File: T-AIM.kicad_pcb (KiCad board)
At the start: 2 copper layers, 87.7 x 68.7 mm, 44 parts, among them IC1 ATMEGA328PB-A, J1 ADXL345 Connector, J2 PIR Sensor Connector, J3 JY-MCU HC-05 Pins, J4 CONN_01X03, J5 CONN_01X02, J6 CONN_01X03, SW1 Connection Button, SW2 Reset Button, U1 TPS61200

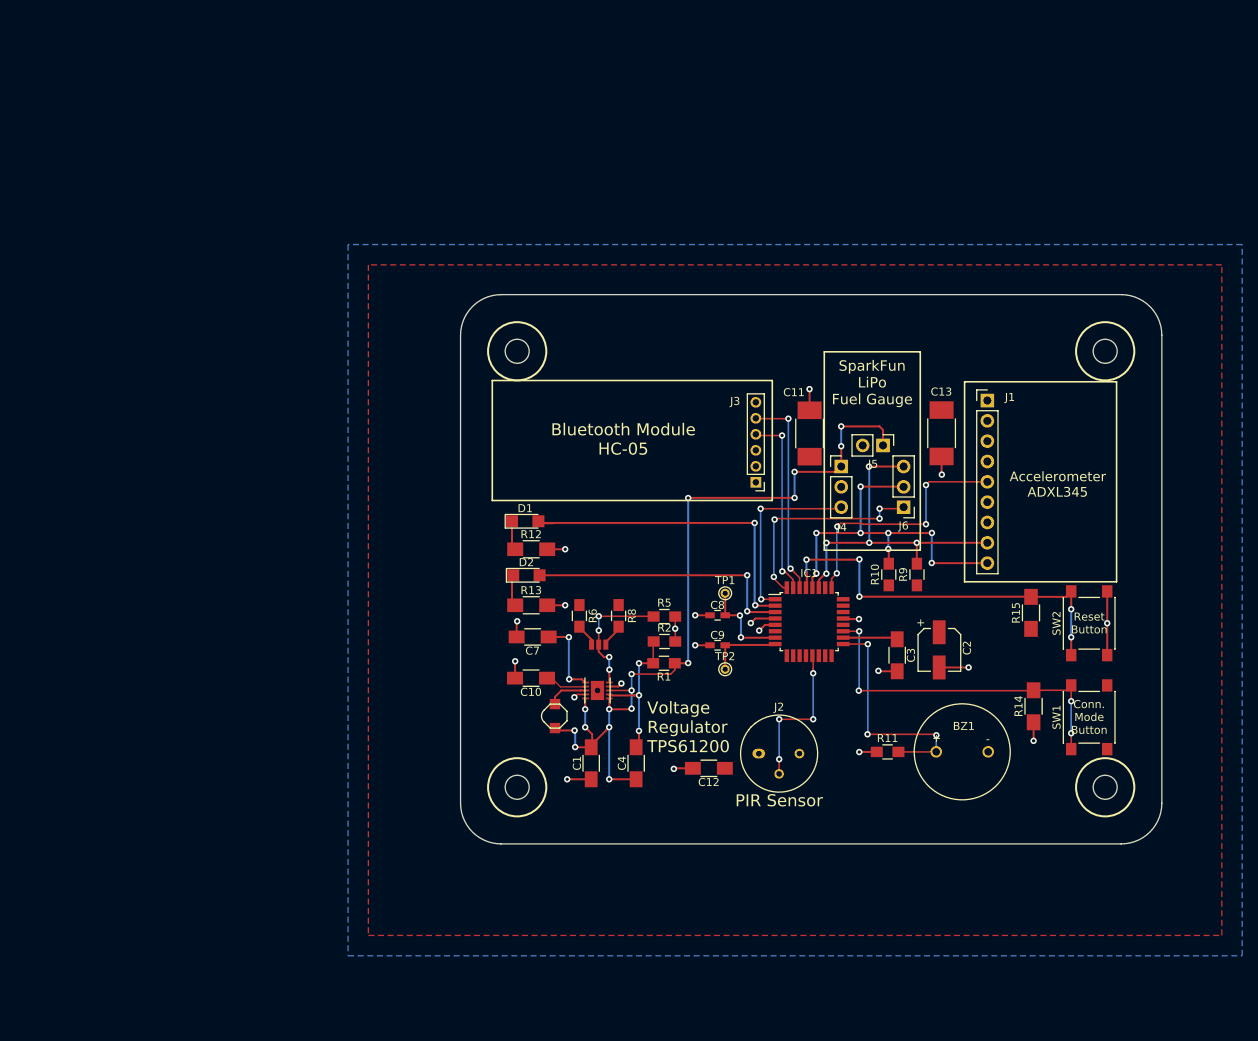
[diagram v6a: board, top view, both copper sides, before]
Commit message: v0.3: 3.9V field shrunk; Added ISP header; Fixed fuel gauge pin shortcut :P
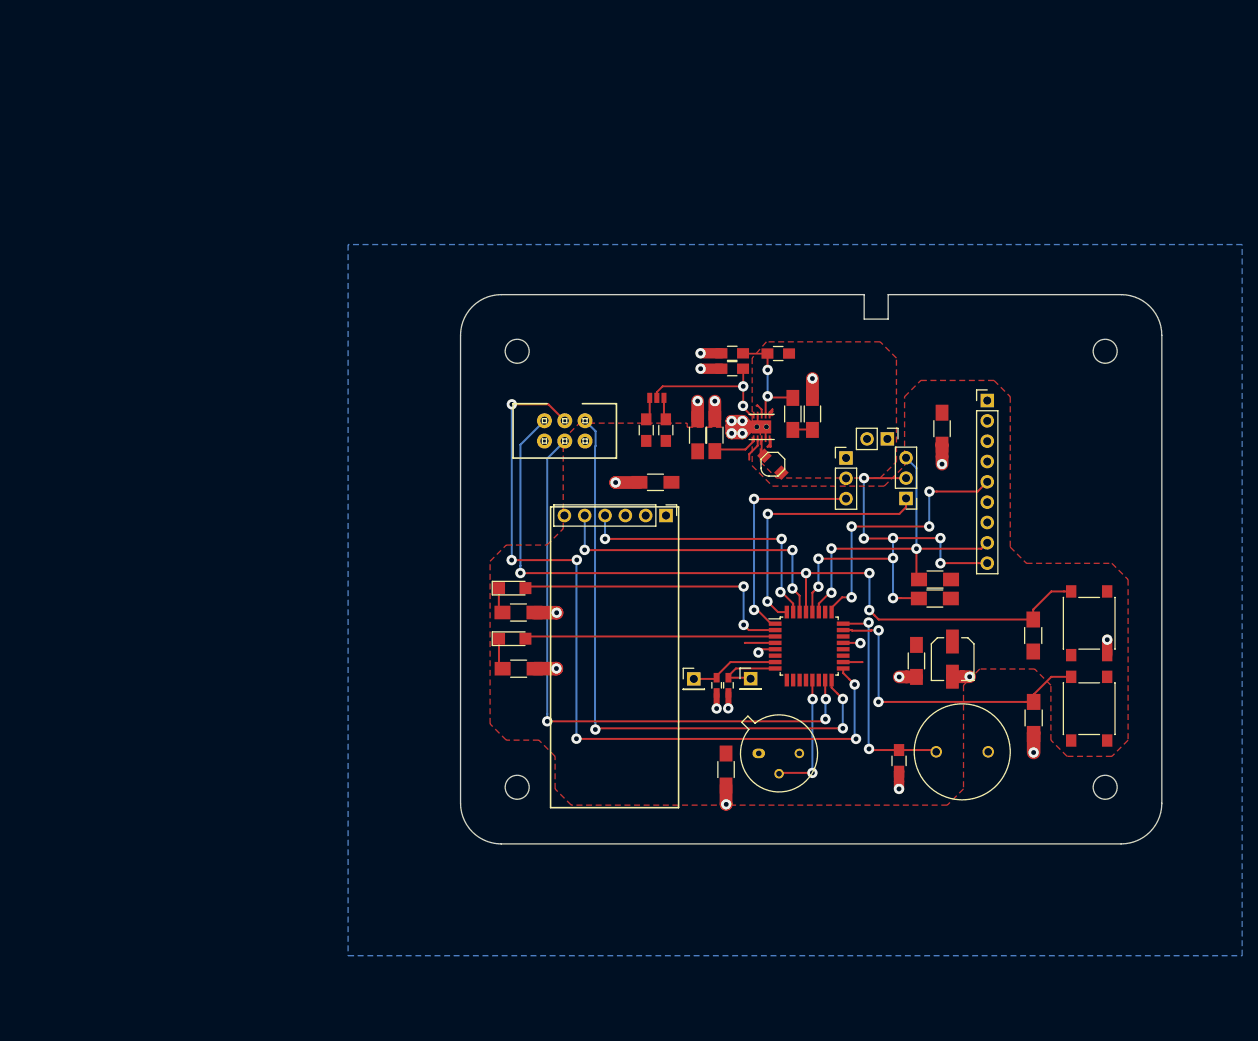
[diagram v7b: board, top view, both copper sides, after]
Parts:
- removed C12: 0.1uF, Capacitors_SMD:C_1206_HandSoldering
- removed C13: 0.1uF, Capacitors_SMD:C_1812_HandSoldering
- removed R13: 220, Resistors_SMD:R_1206_HandSoldering
- removed R14, R15: 10k, Resistors_SMD:R_1206_HandSoldering
- added C5: 0.1uF, Capacitors_SMD:C_1206_HandSoldering, F.Cu at (152.1, 69.8)
- added C6: 22pF, Capacitors_SMD:C_0603_HandSoldering, F.Cu at (152.3, 101.1)
- added CON1: AVR-ISP-6, T-AIM:2X3-SHROUDED, F.Cu at (133.3, 69.3)
- added R3: 220k, Resistors_SMD:R_0805_HandSoldering, F.Cu at (154.2, 61.5)
- added R4: 1.5M, Resistors_SMD:R_0805_HandSoldering, F.Cu at (145.9, 69.2)
- added R7: 10k, Resistors_SMD:R_1206_HandSoldering, F.Cu at (179.6, 90.2)
- C10: value 22uF -> 0.1uF
- C11: footprint Capacitors_SMD:C_1812_HandSoldering -> Capacitors_SMD:C_1206_HandSoldering
- C7: value 0.1uF -> 22pF; footprint Capacitors_SMD:C_1206_HandSoldering -> Capacitors_SMD:C_0603_HandSoldering
- C8: value 22pF -> 22uF; footprint Capacitors_SMD:C_0603_HandSoldering -> Capacitors_SMD:C_1206_HandSoldering
- C9: value 22pF -> 0.1uF; footprint Capacitors_SMD:C_0603_HandSoldering -> Capacitors_SMD:C_1206_HandSoldering
- J1: value ADXL345 Connector -> CONN_01X03; footprint Pin_Headers:Pin_Header_Straight_1x09_Pitch2.54mm -> Pin_Headers:Pin_Header_Straight_1x03_Pitch2.54mm
- J2: value PIR Sensor Connector -> CONN_01X02; footprint T-AIM:TO-5-3 -> Pin_Headers:Pin_Header_Straight_1x02_Pitch2.54mm
- J3: value JY-MCU HC-05 Pins -> CONN_01X03; footprint Pin_Headers:Pin_Header_Straight_1x06_Pitch2.00mm -> Pin_Headers:Pin_Header_Straight_1x03_Pitch2.54mm
- J4: value CONN_01X03 -> ADXL345 Connector; footprint Pin_Headers:Pin_Header_Straight_1x03_Pitch2.54mm -> Pin_Headers:Pin_Header_Straight_1x09_Pitch2.54mm
- J5: value CONN_01X02 -> PIR Sensor Connector; footprint Pin_Headers:Pin_Header_Straight_1x02_Pitch2.54mm -> TO_SOT_Packages_THT:TO-5-3
- J6: value CONN_01X03 -> JY-MCU HC-05 Pins; footprint Pin_Headers:Pin_Header_Straight_1x03_Pitch2.54mm -> Pin_Headers:Pin_Header_Straight_1x06_Pitch2.54mm
- R10, R9: value 10k -> 220; footprint Resistors_SMD:R_0805_HandSoldering -> Resistors_SMD:R_1206_HandSoldering
- R11: value 1M -> 10k; footprint Resistors_SMD:R_0805_HandSoldering -> Resistors_SMD:R_1206_HandSoldering
- R12: value 220 -> 10k
- R5: value 220k -> 2M
- R6: value 1.37M -> 10k; footprint Resistors_SMD:R_0805_HandSoldering -> Resistors_SMD:R_1206_HandSoldering
- R8: value 2M -> 1M
- TP1, TP2: footprint Connectors:PINTST -> Pin_Headers:Pin_Header_Straight_1x01_Pitch2.54mm
- U1: footprint DRC-10-Thermal-Vias -> T-AIM:DRC-10-Thermal-Vias
- moved R12 63.7 mm to (191.8, 94.9), turned to 90 degrees
- moved C1 51.7 mm to (164.2, 67.2), turned to 90 degrees
- moved R9 50.0 mm to (127.5, 92.0), turned to 0 degrees
- moved C4 47.9 mm to (161.8, 67.2)
- moved R10 47.7 mm to (127.5, 99.0), turned to 0 degrees
- moved R6 44.7 mm to (179.6, 87.9), turned to 180 degrees
- moved J2 42.5 mm to (173.6, 70.3), turned to 270 degrees
- moved L1 41.6 mm to (159.3, 73.5), turned to 315 degrees
- moved J5 41.5 mm to (157.5, 109.6), turned to 0 degrees
- moved R1 41.3 mm to (160.0, 59.6)
- moved R8 39.5 mm to (175.1, 110.5), turned to 90 degrees
- moved U1 38.8 mm to (157.9, 68.8), turned to 180 degrees
- moved R2 37.0 mm to (154.2, 59.6), turned to 180 degrees
- moved SJ1 31.7 mm to (144.8, 65.2), turned to 180 degrees
- moved J6 29.7 mm to (145.9, 79.9), turned to 270 degrees
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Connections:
- BZ1 pad 1: AlarmBuzzer -> Alarm
- C10 pad 1: 3V6 -> 3V9
- C11 pad 1: 3V6 -> 3V9
- C2 pad 1: 3V6 -> 3V9
- C3 pad 1: 3V6 -> 3V9
- C8 pad 1: GND -> 3V9
- C8 pad 2: Net-(C8-Pad2) -> GND
- C9 pad 1: Net-(C9-Pad1) -> 3V9
- IC1 pad 15: Net-(IC1-Pad15) -> MOSI
- IC1 pad 16: Net-(IC1-Pad16) -> MISO
- IC1 pad 17: AlarmBuzzer -> SCK
- IC1 pad 18: 3V6 -> 3V9
- IC1 pad 19: ConnectedButton -> Net-(IC1-Pad19)
- IC1 pad 23: Net-(IC1-Pad23) -> ConnBtn
- IC1 pad 24: Net-(IC1-Pad24) -> Alarm
- IC1 pad 29: ResetButton -> RST
- IC1 pad 4: 3V6 -> 3V9
- IC1 pad 7: Net-(C8-Pad2) -> Net-(C6-Pad2)
- IC1 pad 8: Net-(C9-Pad1) -> Net-(C7-Pad1)
- J1 pad 1: 3V6 -> Net-(J1-Pad1)
- J1 pad 2: Net-(J1-Pad2) -> GND
- J1 pad 3: GND -> BatteryLowAlert
- J2 pad 1: 3V6 -> VCC
- J2 pad 2: PIR_OUT -> GND
- J3 pad 1: Net-(J3-Pad1) -> FuelGaugeRestart
- J3 pad 2: 3V6 -> /SCL
- J3 pad 3: GND -> /SDA
- J4 pad 1: VCC -> 3V9
- J4 pad 2: GND -> Net-(J4-Pad2)
- J4 pad 3: BatteryLowAlert -> GND
- J5 pad 1: VCC -> 3V9
- J5 pad 2: GND -> PIR_OUT
- J6 pad 1: FuelGaugeRestart -> Net-(J6-Pad1)
- J6 pad 2: /SCL -> 3V9
- J6 pad 3: /SDA -> GND
- R10 pad 1: 3V6 -> Net-(D2-Pad1)
- R10 pad 2: /SCL -> GND
- R11 pad 2: AlarmBuzzer -> ConnBtn
- R12 pad 1: Net-(D1-Pad1) -> 3V9
- R12 pad 2: GND -> RST
- R5 pad 1: Net-(R5-Pad1) -> 3V9
- R5 pad 2: GND -> /5V
- R6 pad 1: 3V6 -> 3V9
- R6 pad 2: /3.6V -> /SDA
- R8 pad 1: 3V6 -> GND
- R8 pad 2: /5V -> Alarm
- R9 pad 1: 3V6 -> Net-(D1-Pad1)
- R9 pad 2: /SDA -> GND
- SJ1 pad 1: /3.6V -> /3.9V
- SJ1 pad 2: Net-(R5-Pad1) -> Net-(R3-Pad1)
- SW1 pad 1: ConnectedButton -> ConnBtn
- SW1 pad 2: 3V6 -> 3V9
- SW2 pad 1: ResetButton -> RST
- TP1 pad 1: Net-(C8-Pad2) -> Net-(C6-Pad2)
- TP2 pad 1: Net-(C9-Pad1) -> Net-(C7-Pad1)
- U1 pad 1: Net-(C7-Pad1) -> Net-(C5-Pad1)
- U1 pad 10: Net-(R5-Pad1) -> Net-(R3-Pad1)
- U1 pad 2: 3V6 -> 3V9
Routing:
- net SCK: track 0.00 -> 101.9 mm, vias 0 -> 6
- net RST: track 0.00 -> 101.8 mm, vias 0 -> 4
- net VCC: track 103.3 -> 9.52 mm, vias 16 -> 0
- net MISO: track 0.00 -> 76.8 mm, vias 0 -> 3
- net MOSI: track 0.00 -> 75.8 mm, vias 0 -> 3
- net ResetButton: track 51.6 -> 0.00 mm, vias 5 -> 0
- net ConnectedButton: track 45.0 -> 0.00 mm, vias 4 -> 0
- net ConnBtn: track 0.00 -> 41.0 mm, vias 0 -> 2
- net AlarmBuzzer: track 30.5 -> 0.00 mm, vias 3 -> 0
- net Alarm: track 0.00 -> 27.6 mm, vias 0 -> 2
- net Net-(R3-Pad1): track 0.00 -> 19.3 mm, vias 0 -> 2
- net Net-(R5-Pad1): track 17.0 -> 0.00 mm, vias 4 -> 0
- net 3V6: track 15.1 -> 0.00 mm, vias 1 -> 0
- net BL_RXD: track 25.5 -> 38.4 mm, vias 2 -> 3
- net Net-(C8-Pad2): track 11.7 -> 0.00 mm, vias 2 -> 0
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- added copper zone on F.Cu, net 3V9
- added copper zone on F.Cu, net VCC
- removed copper zone on F.Cu, net 3V6
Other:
- outline, holes or cut-outs redrawn
- net class Default: clearance 0.1 -> 0.25; via_dia 0.8 -> 1.3; via_drill 0.4 -> 0.6
- net class EP removed
- net class Power: clearance 0.1 -> 0.25; via_dia 0.8 -> 1.3; via_drill 0.4 -> 0.6
- net class Signal: clearance 0.1 -> 0.25; trace_width 0.2 -> 0.25; via_dia 0.8 -> 1.3; via_drill 0.4 -> 0.6
- rule trace_clearance: 0.1 -> 0.25
- board text added: "3V9"
- board text added: "5V"
- board text added: "ATmega328P"
- board text added: "Alarm Buzzer"
- board text added: "Status LED 1"
- board text added: "Status LED 2"
- board text added: "T-AIM v0.3"
- board text added: "TPS61200 Voltage Regulator"
- board text removed: "T-AIM Sensor Board v0.1"
- board text removed: "Voltage Regulator TPS61200"
